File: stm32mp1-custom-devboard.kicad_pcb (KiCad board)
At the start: 4 copper layers, 120 x 80.6 mm, 194 parts, among them CON1 52746-0671, CON2 505110-2491, CON3 2041119-1, CON4 USB_C_Wurth_632723300011, CON5 USB_C_Wurth_632723300011, CON6 TC2050-IDC-NL-SWI, P1 Main Power Supply, Q1 BC847B, Sw1 434153017835, Sw2 434153017835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

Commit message: Placed all elements on pcb
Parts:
- D2: value VAL** -> BAT54C
- D3: value Val* -> HSMF-C155
- L5: value 4.7uH -> 742792515
- SOM1: value SODIMM_SOCKET_200P_5_1473005-4 -> VisionSOM-STM32MP1
- T2: value >VALUE -> WE-RJ45_74990101210
- U1: value VAL -> TPS61169DCKR
- U4: value NCP708MU330TAG -> ST1S09IPUR
- moved C7 117.1 mm to (204.7, 126.7)
- moved C47 105.2 mm to (192.4, 124.3)
- moved U9 105.2 mm to (190.2, 124.3)
- moved C48 105.2 mm to (187.9, 124.3)
- moved D11 105.1 mm to (142.3, 126.5), turned to -90 degrees
- moved R67 100.7 mm to (136.2, 99.3), turned to 180 degrees
- moved REF1 98.3 mm to (157.0, 89.4)
- moved D10 98.3 mm to (148.9, 126.5), turned to -90 degrees
- moved R70 98.1 mm to (136.2, 100.3), turned to 180 degrees
- moved C33 97.9 mm to (148.8, 89.3), turned to 0 degrees
- moved C34 92.5 mm to (147.0, 91.0)
- moved R40 92.5 mm to (149.6, 92.8)
- moved R64 92.3 mm to (146.2, 100.1), turned to -90 degrees
- moved R37 91.9 mm to (150.4, 97.3), turned to 0 degrees
- moved R39 91.0 mm to (150.4, 98.8), turned to 0 degrees
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
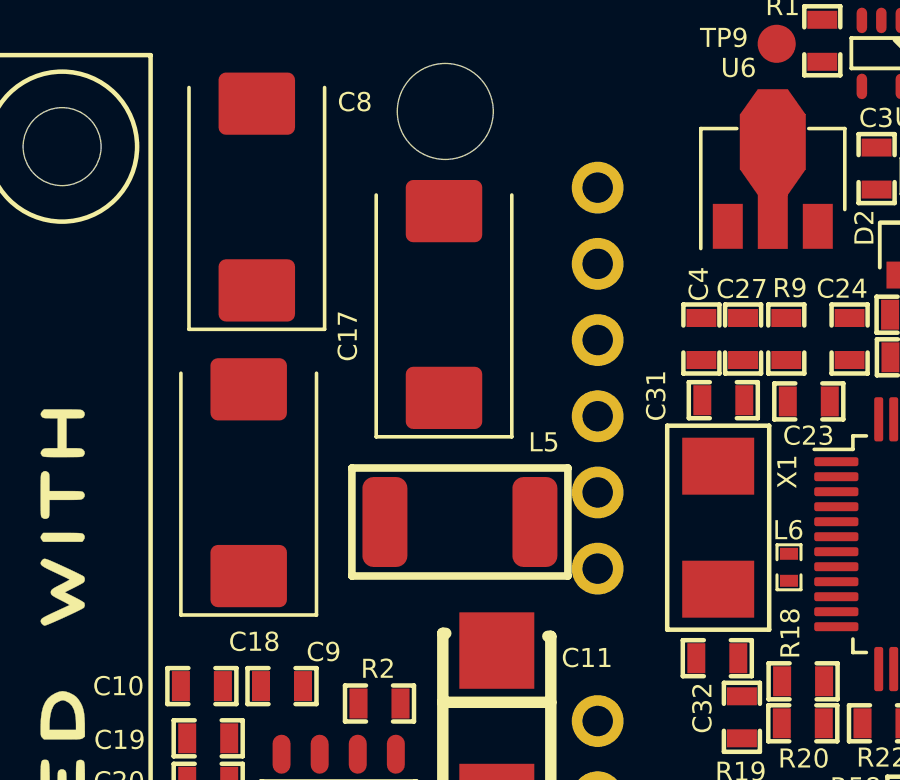
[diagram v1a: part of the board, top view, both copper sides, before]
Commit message: Updated place of capacitor
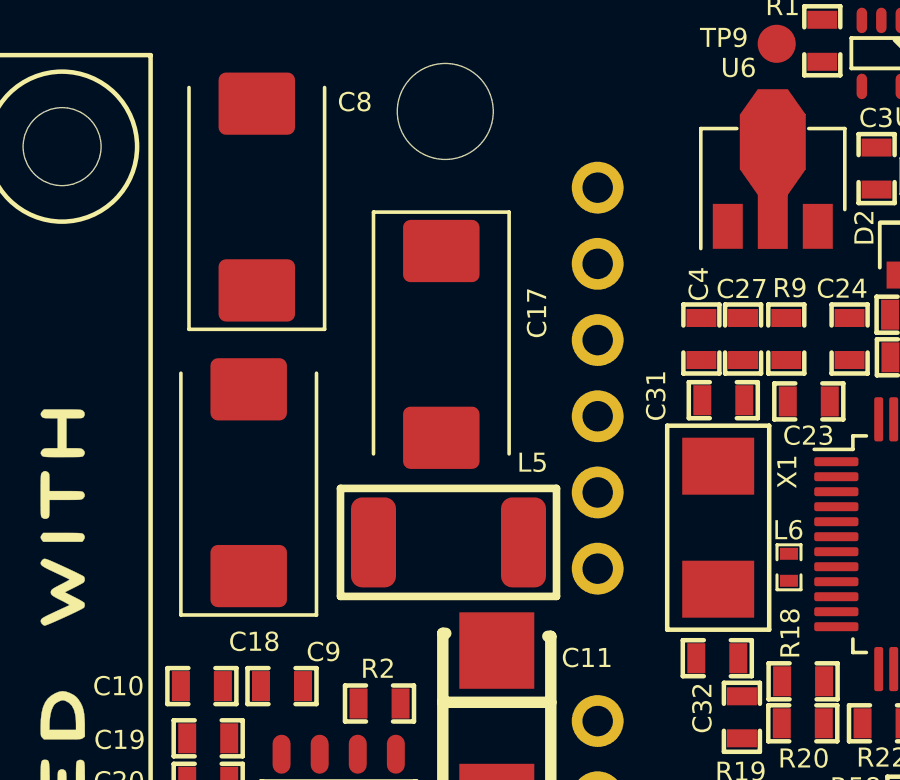
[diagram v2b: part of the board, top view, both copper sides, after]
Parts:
- moved C17 1.33 mm to (177.2, 74.4), turned to -90 degrees
- moved L5 0.78 mm to (177.5, 81.0)
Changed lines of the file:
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@@
   )
   (footprint "Smd_Tantal:22uF_35V_Size_D" (layer "F.Cu")
-    (at 177.33 73.1 90)
+    (at 177.24 74.43 -90)
     (descr "Tantalum Capacitor SMD Kemet-D (7343-31 Metric), IPC_7351 nominal, (Body size from: http://www.kemet.com/Lists/ProductCatalog/Attachments/253/KEM_TC101_STD.pdf), generated with kicad-footprint-generator")
     (tags "capacitor tantalum")
@@
     (property "URL" "https://www.tme.eu/pl/details/293d226x9035d2te3/kondensatory-tantalowe-smd/vishay/")
     (attr smd)
-    (fp_text reference "C17" (at -1.05 -3.2 270) (layer "F.SilkS")
+    (fp_text reference "C17" (at -1.05 -3.2 90) (layer "F.SilkS")
       (effects (font (size 0.635 0.635) (thickness 0.15875)))
     )
@@
     (fp_line (start -2.65 -2.15) (end -3.65 -1.15) (layer "F.Fab") (width 0.1))
     (fp_line (start 3.65 -2.15) (end -2.65 -2.15) (layer "F.Fab") (width 0.1))
-    (pad "1" smd roundrect (at -3.1125 0 90) (size 2.075 2.55) (layers "F.Cu" "F.Paste" "F.Mask") (roundrect_rratio 0.120482)
+    (pad "1" smd roundrect (at -3.1125 0 270) (size 2.075 2.55) (layers "F.Cu" "F.Paste" "F.Mask") (roundrect_rratio 0.120482)
       (net 13 "5V") (pintype "input"))
-    (pad "2" smd roundrect (at 3.1125 0 90) (size 2.075 2.55) (layers "F.Cu" "F.Paste" "F.Mask") (roundrect_rratio 0.120482)
+    (pad "2" smd roundrect (at 3.1125 0 270) (size 2.075 2.55) (layers "F.Cu" "F.Paste" "F.Mask") (roundrect_rratio 0.120482)
       (net 1 "GND") (pintype "input"))
     (model "${KISYS3DMOD}/Capacitors/Smd_Tantal/3D_View/22uF_35V_Size_D.wrl"
@@
   )
   (footprint "Inductors:742792515" (layer "F.Cu")
-    (at 177.86 80.35)
+    (at 177.48 81.03)
     (descr "Ferrite Beads WE-CBF 1812 SMD Bead 100MHz 785Ohm 3A")
     (tags "SMD Inductor")

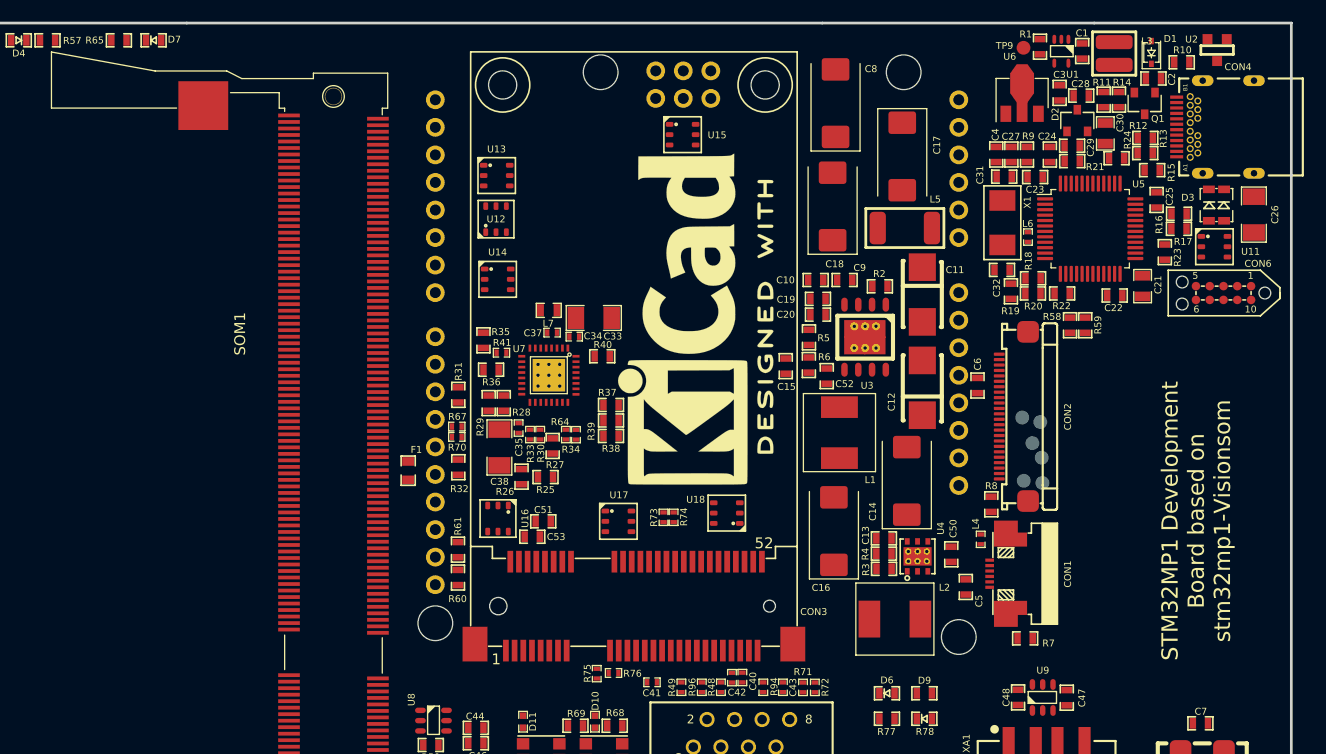
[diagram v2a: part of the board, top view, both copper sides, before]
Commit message: Replaced some elements on pcb
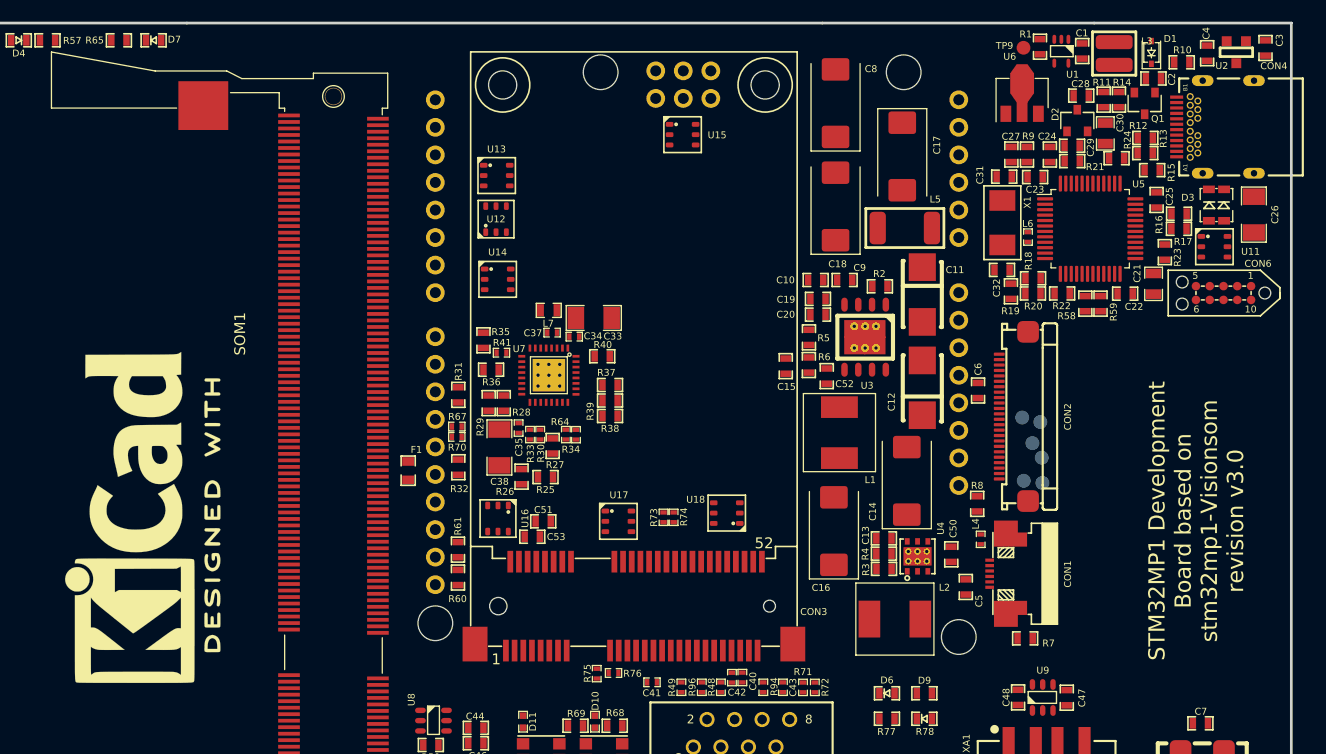
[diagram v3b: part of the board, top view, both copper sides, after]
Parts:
- moved REF1 54.2 mm to (106.0, 107.7)
- moved C4 21.6 mm to (205.3, 64.9)
- moved C3 19.4 mm to (210.7, 64.4)
- moved R58 2.44 mm to (194.1, 88.0)
- moved R59 2.44 mm to (195.5, 88.0)
- moved R37 1.84 mm to (150.3, 95.5)
- moved R38 1.84 mm to (150.3, 98.4)
- moved R39 1.84 mm to (150.3, 96.9)
- moved U2 1.78 mm to (208.0, 64.8)
- moved R8 1.30 mm to (184.2, 106.5)
- moved C21 1.03 mm to (200.4, 86.2)
- moved C22 0.97 mm to (197.8, 87.1)
- moved C6 0.46 mm to (184.2, 96.0)
- moved C18 0.27 mm to (171.1, 79.0)
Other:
- board text added: "STM32MP1 Development Board based on stm32mp1-Visionsom revision v3.0"
- board text removed: "STM32MP1 Development Board based on stm32mp1-Visionsom"
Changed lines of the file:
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@@
   )
   (footprint "Capacitors_Smd_0603:100nF_0603" (layer "F.Cu")
-    (at 184.18 95.55 90)
+    (at 184.23 96.01 90)
     (descr "Vishay SMD SM0603")
     (tags "Capacitor")
@@
       (effects (font (size 0.635 0.635) (thickness 0.15)))
     )
-    (fp_line (start 0.75 0.4) (end 0.75 -0.4) (layer "F.SilkS") (width 0.1))
+    (fp_line (start -0.75 0.4) (end -0.75 -0.4) (layer "F.SilkS") (width 0.1))
     (fp_line (start 0.75 -0.4) (end 0.25 -0.4) (layer "F.SilkS") (width 0.1))
-    (fp_line (start -0.25 -0.4) (end -0.75 -0.4) (layer "F.SilkS") (width 0.1))
-    (fp_line (start -0.75 0.4) (end -0.25 0.4) (layer "F.SilkS") (width 0.1))
     (fp_line (start 0.25 0.4) (end 0.75 0.4) (layer "F.SilkS") (width 0.1))
-    (fp_line (start -0.75 0.4) (end -0.75 -0.4) (layer "F.SilkS") (width 0.1))
-    (fp_line (start -0.5 -0.25) (end 0.5 -0.25) (layer "F.Fab") (width 0.1))
-    (fp_line (start 0.5 -0.25) (end 0.5 0.25) (layer "F.Fab") (width 0.1))
+    (fp_line (start -0.75 0.4) (end -0.25 0.4) (layer "F.SilkS") (width 0.1))
+    (fp_line (start -0.25 -0.4) (end -0.75 -0.4) (layer "F.SilkS") (width 0.1))
+    (fp_line (start 0.75 0.4) (end 0.75 -0.4) (layer "F.SilkS") (width 0.1))
     (fp_line (start 0.5 0.25) (end -0.5 0.25) (layer "F.Fab") (width 0.1))
+    (fp_line (start -0.5 -0.25) (end 0.5 -0.25) (layer "F.Fab") (width 0.1))
     (fp_line (start -0.5 0.25) (end -0.5 -0.25) (layer "F.Fab") (width 0.1))
-    (pad "1" smd rect locked (at -0.45 0 270) (size 0.4 0.6) (layers "F.Cu" "F.Paste" "F.Mask")
+    (fp_line (start 0.5 -0.25) (end 0.5 0.25) (layer "F.Fab") (width 0.1))
+    (pad "1" smd rect (at -0.45 0 270) (size 0.4 0.6) (layers "F.Cu" "F.Paste" "F.Mask")
       (net 4 "Net-(C6-Pad1)") (pinfunction "1") (pintype "passive") (solder_mask_margin 0.03) (clearance 0.07))
-    (pad "2" smd rect locked (at 0.45 0 270) (size 0.4 0.6) (layers "F.Cu" "F.Paste" "F.Mask")
+    (pad "2" smd rect (at 0.45 0 270) (size 0.4 0.6) (layers "F.Cu" "F.Paste" "F.Mask")
       (net 3 "/LCD+Touchscreen/Touchscreen Power Supply/VOUT_3.3V_250mA") (pinfunction "2") (pintype "passive") (solder_mask_margin 0.03) (clearance 0.07))
-    (model "${KISYS3DMOD}/Inductors/3D_View/BLM15HG601SN1D.x3d"
+    (model "${KISYS3DMOD}/Inductors/3D_View/BLM15HG601SN1D.wrl"
       (offset (xyz 0 0 0))
       (scale (xyz 1 1 1))
@@
   )
   (footprint "Smd_Tantal:22uF_35V_Size_D" (layer "F.Cu")
-    (at 170.82 79.04 90)
+    (at 171.09 79.04 90)
     (descr "Tantalum Capacitor SMD Kemet-D (7343-31 Metric), IPC_7351 nominal, (Body size from: http://www.kemet.com/Lists/ProductCatalog/Attachments/253/KEM_TC101_STD.pdf), generated with kicad-footprint-generator")
     (tags "capacitor tantalum")
@@
   )
   (footprint "Resistor_Smd_0603:4k7_0603" (layer "F.Cu")
-    (at 185.45 106.5 90)
+    (at 184.15 106.46 90)
     (descr "Vishay SMD SM0603")
     (tags "Resistor")
@@
   )
   (footprint "Capacitors_Smd_0805:10uF_0805" (layer "F.Cu")
-    (at 199.4 86.38 90)
+    (at 200.41 86.17 90)
     (tags "Capacitor")
     (property "Developer" "MW")
@@
     (solder_paste_margin -0.1)
     (attr smd)
-    (fp_text reference "C21" (at 0.12 1.43 90) (layer "F.SilkS")
+    (fp_text reference "C21" (at 0.96 -1.51 90) (layer "F.SilkS")
       (effects (font (size 0.635 0.635) (thickness 0.127)))
     )
@@
   )
   (footprint "Capacitors_Smd_0603:100nF_0603" (layer "F.Cu")
-    (at 196.83 87.25 180)
+    (at 197.79 87.08 180)
     (descr "Vishay SMD SM0603")
     (tags "Capacitor")
@@
     (property "URL" "https://www.tme.eu/pl/details/cl10b104jb8nnnc/kondensatory-mlcc-smd-0603/samsung/")
     (attr smd)
-    (fp_text reference "C22" (at 0.11 -1.14 180) (layer "F.SilkS")
+    (fp_text reference "C22" (at -0.82 -1.2 180) (layer "F.SilkS")
       (effects (font (size 0.635 0.635) (thickness 0.127)))
     )
@@
   )
   (footprint "Capacitors_Smd_0603:1uF_0603" (layer "F.Cu")
-    (at 185.91 74.25 -90)
+    (at 205.35 64.91 -90)
     (descr "Vishay SMD SM0603")
     (tags "Capacitor")
@@
   )
   (footprint "Resistor_Smd_0603:1k_0603" (layer "F.Cu")
-    (at 150.39 97.34)
+    (at 150.3 95.5)
     (descr "Vishay SMD SM0603")
     (tags "Resistor")
@@
   )
   (footprint "Linear:MCP1703T-3302E_SOT23" (layer "F.Cu")
-    (at 206.27 64.62)
+    (at 208.04 64.82)
     (descr "MCP1703T-3302E")
     (tags "DC-DC LDO Linear Regulator")
@@
     (property "URL" "https://www.tme.eu/pl/details/mcp1703t3302ecb/stabilizatory-napiecia-nieregulowane-ldo/microchip-technology/mcp1703t-3302e-cb/")
     (attr smd)
-    (fp_text reference "U2" (at -2.36 -0.99 180) (layer "F.SilkS")
+    (fp_text reference "U2" (at -1.34 1.25 180) (layer "F.SilkS")
       (effects (font (size 0.635 0.635) (thickness 0.15875)))
     )
@@
   )
   (footprint "Resistor_Smd_0603:10k_0603" (layer "F.Cu")
-    (at 192.71 89.99 90)
+    (at 194.12 88 90)
     (descr "Vishay SMD SM0603")
     (tags "Resistor")
@@
     (solder_paste_margin -0.06)
     (attr smd)
-    (fp_text reference "R58" (at 0.79 -1.66) (layer "F.SilkS")
+    (fp_text reference "R58" (at -1.14 -1.73) (layer "F.SilkS")
       (effects (font (size 0.635 0.635) (thickness 0.127)))
     )
@@
   )
   (footprint "Symbols:KiCad-Logo2_12mm_SilkScreen" locked (layer "F.Cu")
-    (at 156.967106 89.434893 90)
+    (at 105.987106 107.724893 90)
     (descr "KiCad Logo")
     (tags "Logo KiCad")
@@
   )
   (footprint "Resistor_Smd_0603:10k_0603" (layer "F.Cu")
-    (at 194.11 89.99 90)
+    (at 195.52 88 90)
     (descr "Vishay SMD SM0603")
     (tags "Resistor")
@@
     (solder_paste_margin -0.06)
     (attr smd)
-    (fp_text reference "R59" (at 0.02 1.18 90) (layer "F.SilkS")
+    (fp_text reference "R59" (at -0.77 1.2 90) (layer "F.SilkS")
       (effects (font (size 0.635 0.635) (thickness 0.127)))
     )
@@
   )
   (footprint "Resistor_Smd_0603:1k_0603" (layer "F.Cu")
-    (at 150.39 98.77)
+    (at 150.3 96.93)
     (descr "Vishay SMD SM0603")
     (tags "Resistor")
@@
     (property "URL" "https://pl.mouser.com/ProductDetail/Wurth-Elektronik/632723300011?qs=NK6InXoXhq4%252B5eM1PePLPg%3D%3D")
     (attr through_hole)
-    (fp_text reference "CON4" (at 5.159991 -1.519992 180) (layer "F.SilkS")
+    (fp_text reference "CON4" (at 5.249991 1.780008 180) (layer "F.SilkS")
       (effects (font (size 0.635 0.635) (thickness 0.15875)) (justify left bottom))
     )
@@
   )
   (footprint "Resistor_Smd_0603:4k7_0603" (layer "F.Cu")
-    (at 150.39 100.2 180)
+    (at 150.3 98.36 180)
     (descr "Vishay SMD SM0603")
     (tags "Resistor")
@@
   )
   (footprint "Capacitors_Smd_0603:1uF_0603" (layer "F.Cu")
-    (at 191.75 68.57 90)
+    (at 210.73 64.43 90)
     (descr "Vishay SMD SM0603")
     (tags "Capacitor")
@@
     (property "URL" "https://www.tme.eu/pl/details/cl10b105ko8nnnc/kondensatory-mlcc-smd-0603/samsung/")
     (attr smd)
-    (fp_text reference "C3" (at 1.68 -0.01 180) (layer "F.SilkS")
+    (fp_text reference "C3" (at 0.71 1.29 270) (layer "F.SilkS")
       (effects (font (size 0.635 0.635) (thickness 0.127)))
     )
@@
     (effects (font (size 1 1) (thickness 0.25)) (justify mirror))
   )
-  (gr_text "STM32MP1 Development\nBoard based on \nstm32mp1-Visionsom" (at 204.35 108.03 90) (layer "F.SilkS")
+  (gr_text "STM32MP1 Development\nBoard based on \nstm32mp1-Visionsom\nrevision v3.0" (at 204.35 108.03 90) (layer "F.SilkS")
     (effects (font (size 1.5 1.5) (thickness 0.3)))
   )

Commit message: Tracking in progress
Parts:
- moved U12 42.5 mm to (134.5, 122.3)
- moved R43 1.51 mm to (149.0, 139.2), turned to 90 degrees
- moved R28 1.42 mm to (139.1, 97.1)
- moved R29 1.36 mm to (140.5, 97.1)
- moved L6 0.93 mm to (188.8, 82.8), turned to -90 degrees
- turned D9 to 180 degrees
- turned R17 to 180 degrees
- turned R74 to -90 degrees
- turned U18 to 180 degrees
- turned U9 to 180 degrees
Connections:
- U11 pad 3: /STLink Module/STM-JTCK-SWCLK -> /STLink Module/STM-JTMS-~{RESET}
- U9 pad 1: /STM32MP1 module/USB-OTG1-D_N -> /STM32MP1 module/USB-OTG1-D_P
- U9 pad 3: /STM32MP1 module/USB-OTG1-D_P -> /STM32MP1 module/USB-OTG1-D_N
- USB1 pad 2: Net-(U9-Pad6) -> Net-(U9-Pad4)
- USB1 pad 3: Net-(U9-Pad4) -> Net-(U9-Pad6)
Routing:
- net 3V3: track 0.00 -> 87.5 mm, vias 0 -> 46
- net 5V: track 0.00 -> 58.5 mm, vias 0 -> 1
- net /STLink Module/STM-JTMS-~{RESET}: track 0.00 -> 33.3 mm, vias 0 -> 4
- net /STLink Module/STM-JTCK-SWCLK: track 0.00 -> 24.1 mm, vias 0 -> 3
- net /STLink Module/STM-JTMS-SWDIO: track 0.00 -> 23.5 mm, vias 0 -> 4
- net Net-(C45-Pad2): track 0.00 -> 21.6 mm
- net Net-(C49-Pad2): track 0.00 -> 20.7 mm
- net Net-(C26-Pad2): track 0.00 -> 20.2 mm
- net Net-(R51-Pad2): track 0.00 -> 18.6 mm, vias 0 -> 2
- net /MiniPci Module/SPI_SCK: track 0.00 -> 17.4 mm, vias 0 -> 2
- net Net-(R47-Pad1): track 0.00 -> 17.4 mm
- net /MiniPci Module/SPI_GSN: track 0.00 -> 16.0 mm, vias 0 -> 2
- net Net-(R53-Pad2): track 0.00 -> 14.8 mm
- net /MiniPci Module/SPI_MISO: track 0.00 -> 14.1 mm, vias 0 -> 2
- net Net-(R20-Pad1): track 0.00 -> 13.9 mm, vias 0 -> 2
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- added copper zone on In1.Cu, net 3V3
- removed copper zone on In1.Cu, net 5V
